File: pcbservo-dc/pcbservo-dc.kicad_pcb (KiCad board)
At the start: 4 copper layers, 86 parts, among them IC1 NC7WZ241K8X, IC2 NC7WZ241K8X, IC3 NC7WZ241K8X, J1 Conn_01x02, J10 Conn_01x03, J12 Conn_01x02, J13 Conn_01x02, J14 R-78B5.0-2.0, J2 Conn_01x02, J3 BU33SD5WG-TR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

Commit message: en train de router
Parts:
- moved J14 5.19 mm to (212.5, 68.1), turned to 90 degrees
- moved C16 3.01 mm to (208.2, 87.0), turned to 180 degrees
- moved L2 1.18 mm to (206.1, 79.3)
- moved J7 1.10 mm to (170.5, 70.7)
- moved U17 0.23 mm to (179.7, 74.3)
- moved D1 0.07 mm to (210.1, 96.8), turned to -90 degrees
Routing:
- net +3.3V: track 0.00 -> 38.0 mm
- net AO1: track 0.00 -> 31.3 mm, vias 0 -> 2
- net +25V: track 0.00 -> 26.5 mm, vias 0 -> 2
- net /regulateur de tension/SW: track 0.00 -> 25.0 mm, vias 0 -> 2
- net AO2: track 0.00 -> 18.7 mm, vias 0 -> 2
- net NRST: track 0.00 -> 17.0 mm, vias 0 -> 2
- net Net-(J5-Pin_2): track 0.00 -> 11.0 mm
- net Net-(J10-Pin_2): track 0.00 -> 10.9 mm
- net Net-(J4-Pin_2): track 0.00 -> 10.7 mm
- net BO1: track 0.00 -> 9.64 mm
- net Osc_OUT: track 0.00 -> 7.01 mm
- net Net-(D2-K): track 0.00 -> 6.82 mm
- net Net-(D3-K): track 0.00 -> 6.66 mm
- net Net-(D4-K): track 0.00 -> 6.62 mm
- net BO2: track 0.00 -> 6.01 mm
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- added copper zone on B.Cu, net (none)
- added copper zone on F.Cu, net (none)

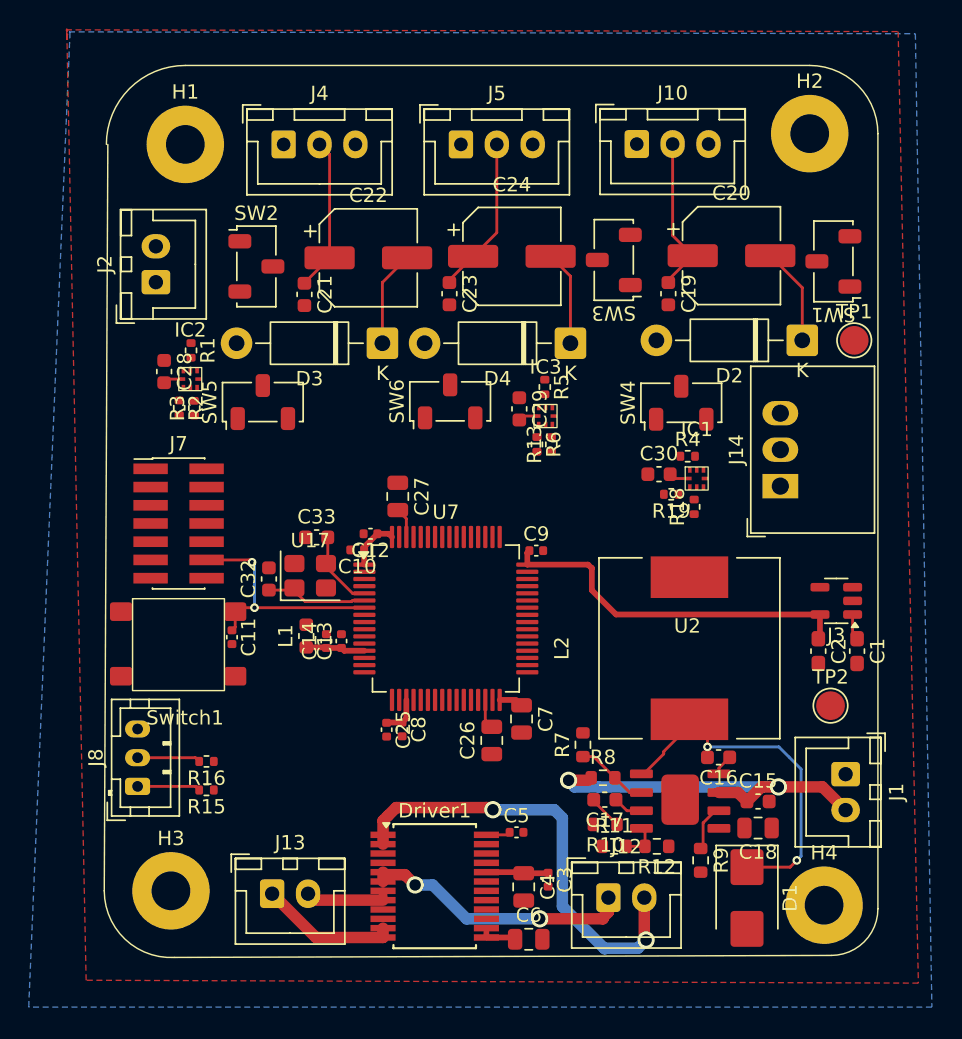
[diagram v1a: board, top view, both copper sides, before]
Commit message: le retouage est bientot fini , il reste que les petit signaus rx tx et configuere l horloge externe et power
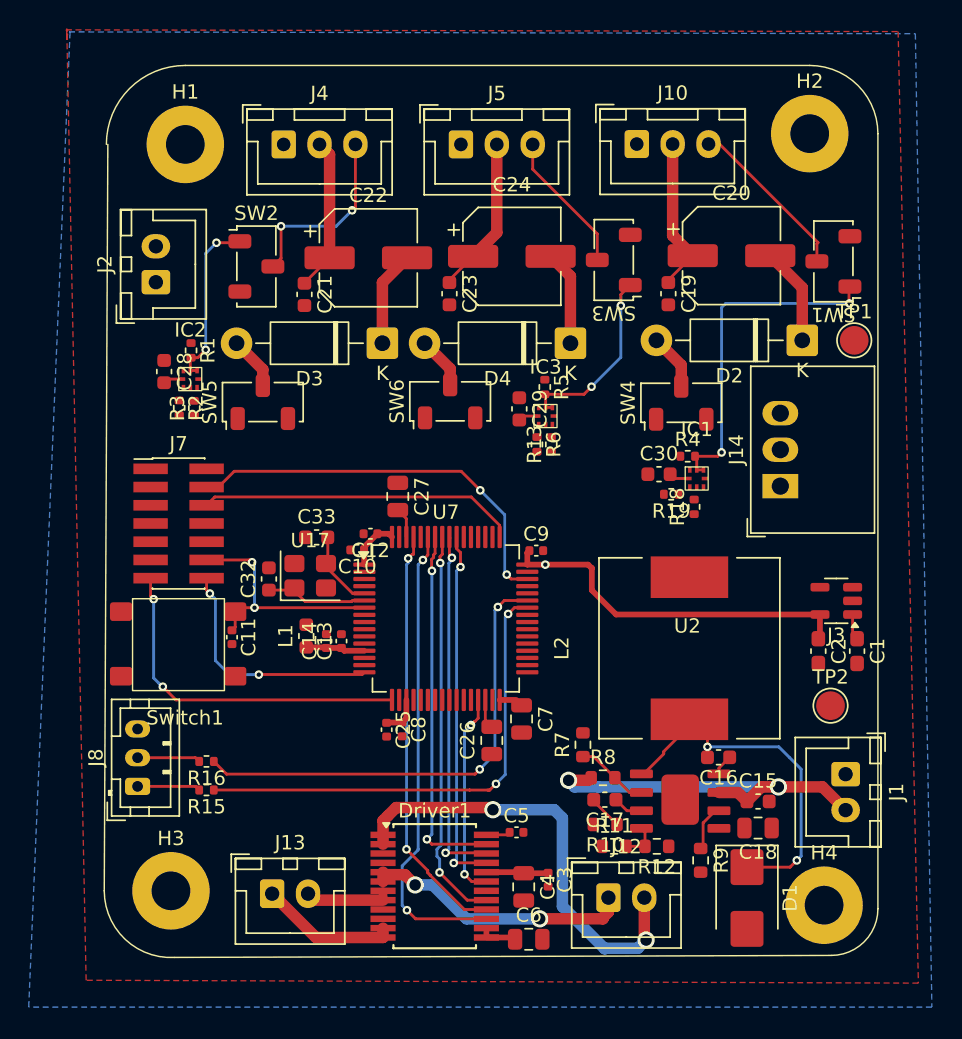
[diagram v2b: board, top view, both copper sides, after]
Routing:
- net USART1_TX: track 0.00 -> 33.7 mm, vias 0 -> 2
- net USART1_RX: track 0.00 -> 33.1 mm, vias 0 -> 2
- net PWMB: track 0.00 -> 32.7 mm, vias 0 -> 2
- net BIN2: track 0.00 -> 29.4 mm, vias 0 -> 2
- net SWDIO: track 0.00 -> 28.3 mm, vias 0 -> 2
- net BIN1: track 0.00 -> 27.7 mm, vias 0 -> 2
- net PWMA: track 0.00 -> 25.8 mm, vias 0 -> 2
- net AIN1: track 0.00 -> 25.3 mm, vias 0 -> 2
- net AIN2: track 0.00 -> 25.2 mm, vias 0 -> 2
- net STLINK_RX: track 0.00 -> 24.7 mm, vias 0 -> 2
- net DXL_PWR1: track 0.00 -> 23.9 mm, vias 0 -> 2
- net SWCLK: track 0.00 -> 22.3 mm
- net STLINK_TX: track 0.00 -> 16.8 mm, vias 0 -> 2
- net STBY: track 0.00 -> 14.8 mm, vias 0 -> 2
- net DXL_PWR3: track 0.00 -> 13.7 mm, vias 0 -> 2
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
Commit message: fin de routage mais correction des erreur
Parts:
- moved SW4 1.16 mm to (204.4, 62.6), turned to 0 degrees
- moved C5 0.56 mm to (193.7, 91.7), turned to 90 degrees
- moved SW5 0.53 mm to (176.6, 62.7), turned to 0 degrees
- moved SW6 0.51 mm to (189.4, 62.7), turned to 0 degrees
- moved C30 0.28 mm to (203.7, 67.2)
- moved C25 0.24 mm to (184.8, 85.0)
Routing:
- net +6V: track 4.39 -> 142.6 mm, vias 0 -> 8
- net +3.3V: track 38.0 -> 170.9 mm, vias 1 -> 8
- net +5V: track 1.82 -> 108.9 mm, vias 0 -> 2
- net PWM1: track 0.00 -> 64.9 mm, vias 0 -> 2
- net TX1_Enable_5V: track 0.00 -> 62.0 mm, vias 0 -> 2
- net TX2_Enable_5V: track 0.00 -> 53.9 mm, vias 0 -> 3
- net +?V: track 0.00 -> 49.3 mm, vias 0 -> 3
- net RXD2_5V: track 0.00 -> 47.8 mm, vias 0 -> 2
- net TXD2_5V: track 0.00 -> 47.2 mm, vias 0 -> 2
- net TXD1_5V: track 0.00 -> 43.2 mm, vias 0 -> 4
- net TX3_Enable_5V: track 0.00 -> 41.5 mm, vias 0 -> 4
- net RXD1_5V: track 0.00 -> 40.9 mm, vias 0 -> 4
- net PWM2: track 0.00 -> 37.9 mm, vias 0 -> 4
- net PWM3: track 0.00 -> 32.1 mm, vias 0 -> 2
- net RXD3_5V: track 0.00 -> 24.1 mm, vias 0 -> 2
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- added copper zone on In2.Cu, net +3.3V
- added copper zone on In2.Cu, net +6V
- added copper zone on In2.Cu, net +?V

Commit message: résolution des erreurs
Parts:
- TP1, TP2: footprint TestPoint:TestPoint_Pad_D2.0mm -> TestPoint:TestPoint_Pad_D1.0mm
- moved TP2 10.5 mm to (215.1, 72.8)
- moved J1 2.94 mm to (218.5, 85.6)
- moved U17 2.80 mm to (177.8, 72.2), turned to 45 degrees
- moved C32 1.98 mm to (178.6, 75.4), turned to -135 degrees
- moved C15 1.76 mm to (211.2, 88.3), turned to 90 degrees
- moved H3 1.75 mm to (170.0, 98.0)
- moved C33 1.72 mm to (180.8, 73.2), turned to -135 degrees
- moved H2 1.58 mm to (216.0, 44.0)
- moved C12 1.34 mm to (183.2, 70.2)
- moved C10 1.28 mm to (183.2, 71.2)
- moved H1 1.03 mm to (170.0, 44.0)
- moved H4 0.90 mm to (216.0, 98.0)
- moved R4 0.36 mm to (206.3, 66.0)
- moved C6 0.28 mm to (194.9, 99.9)
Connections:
- J14 pad 1: +6V -> +25V
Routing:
- net +6V: track 142.6 -> 19.4 mm
- net +3.3V: track 170.9 -> 76.2 mm
- net +?V: track 49.3 -> 5.63 mm
- net GND: track 0.00 -> 22.3 mm, vias 85 -> 75
- net AO1: track 31.2 -> 19.0 mm
- net BO1: track 9.64 -> 0.00 mm
- net +25V: track 26.5 -> 20.0 mm
- net BO2: track 6.01 -> 0.00 mm
- net /regulateur de tension/SW: track 25.8 -> 31.2 mm
- net AO2: track 18.7 -> 15.8 mm
- net Osc_IN: track 5.52 -> 8.26 mm
- net +5V: track 108.9 -> 110.2 mm
- net Alim_servo2: track 5.90 -> 7.18 mm
- net TX2_Enable_5V: track 53.9 -> 53.2 mm, vias 3 -> 2
- net DXL_PWR3: track 13.7 -> 13.1 mm
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- added copper zone on F.Cu, net +25V
- added copper zone on In2.Cu, net +25V
- added copper zone on F.Cu, net +6V
- added copper zone on F.Cu, net AO1
- added copper zone on F.Cu, net AO2
- added copper zone on F.Cu, net BO1
- added copper zone on F.Cu, net BO2
- added copper zone on B.Cu, net GND
- added copper zone on F.Cu, net GND
- removed copper zone on B.Cu, net (none)
- removed copper zone on F.Cu, net (none)
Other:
- board outline added: 58 x 66 mm

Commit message: version finale
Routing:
- net GND: track 22.3 -> 34.3 mm, vias 75 -> 79
